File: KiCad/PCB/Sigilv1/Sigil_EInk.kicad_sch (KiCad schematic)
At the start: 6 parts, among them J2 INLAND E-PAPER HEADER (8-PIN), J3 BUZZER LOGICAL ONLY, J4 ANALOG JOYSTICK HEADER (5-PIN), J5 NEOPIXEL JEWEL 7 RGBW, U1 REMOVABLE ESP32 DEVKIT / 2 x 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

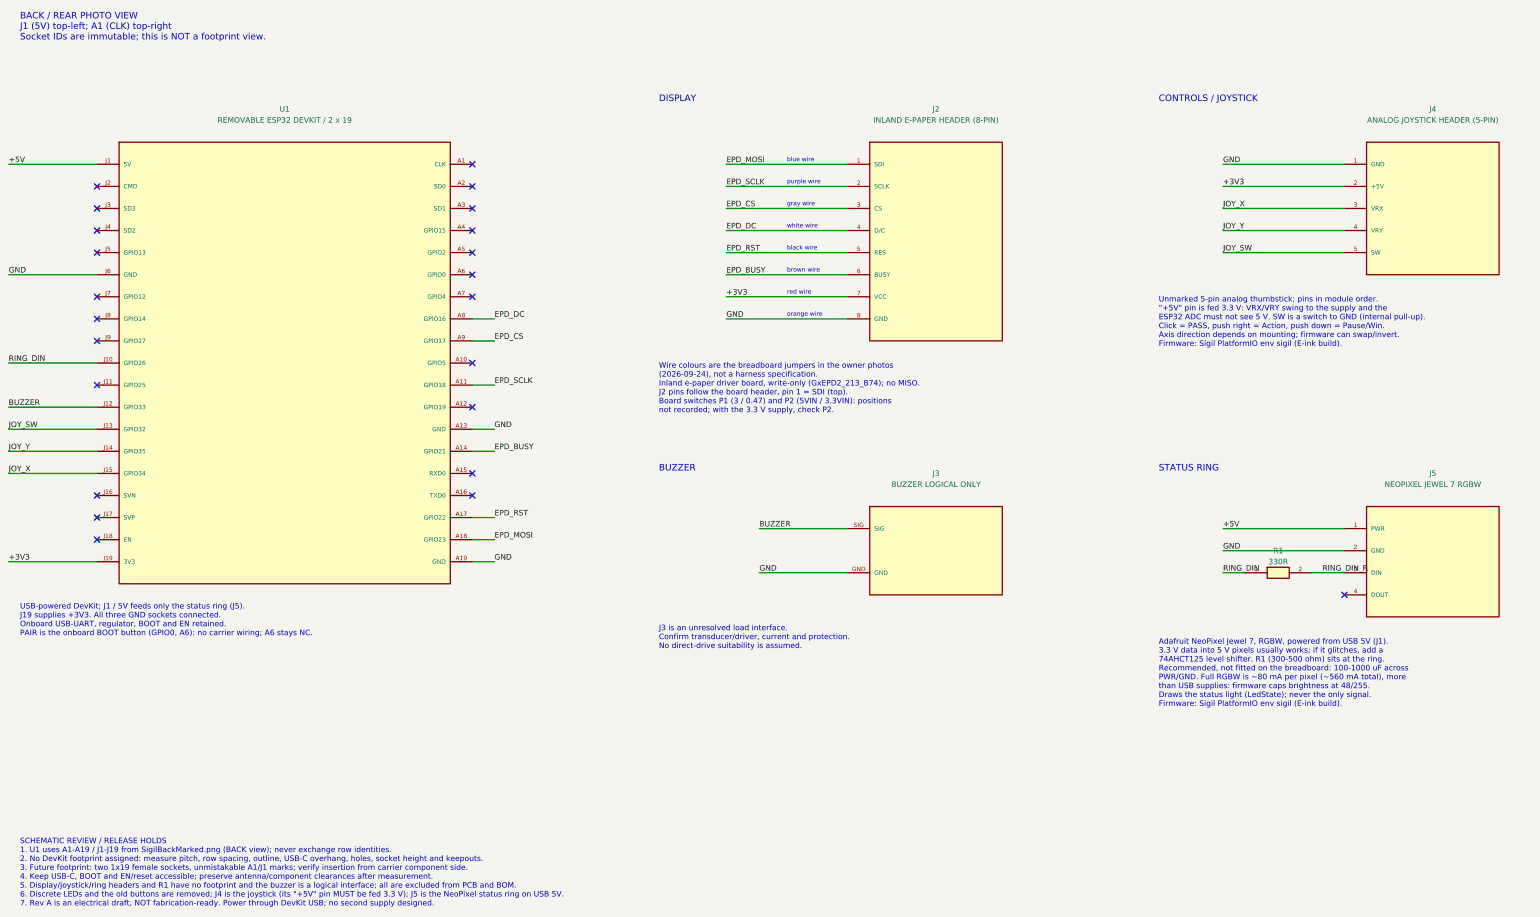
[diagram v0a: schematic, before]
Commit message: New LED Ring
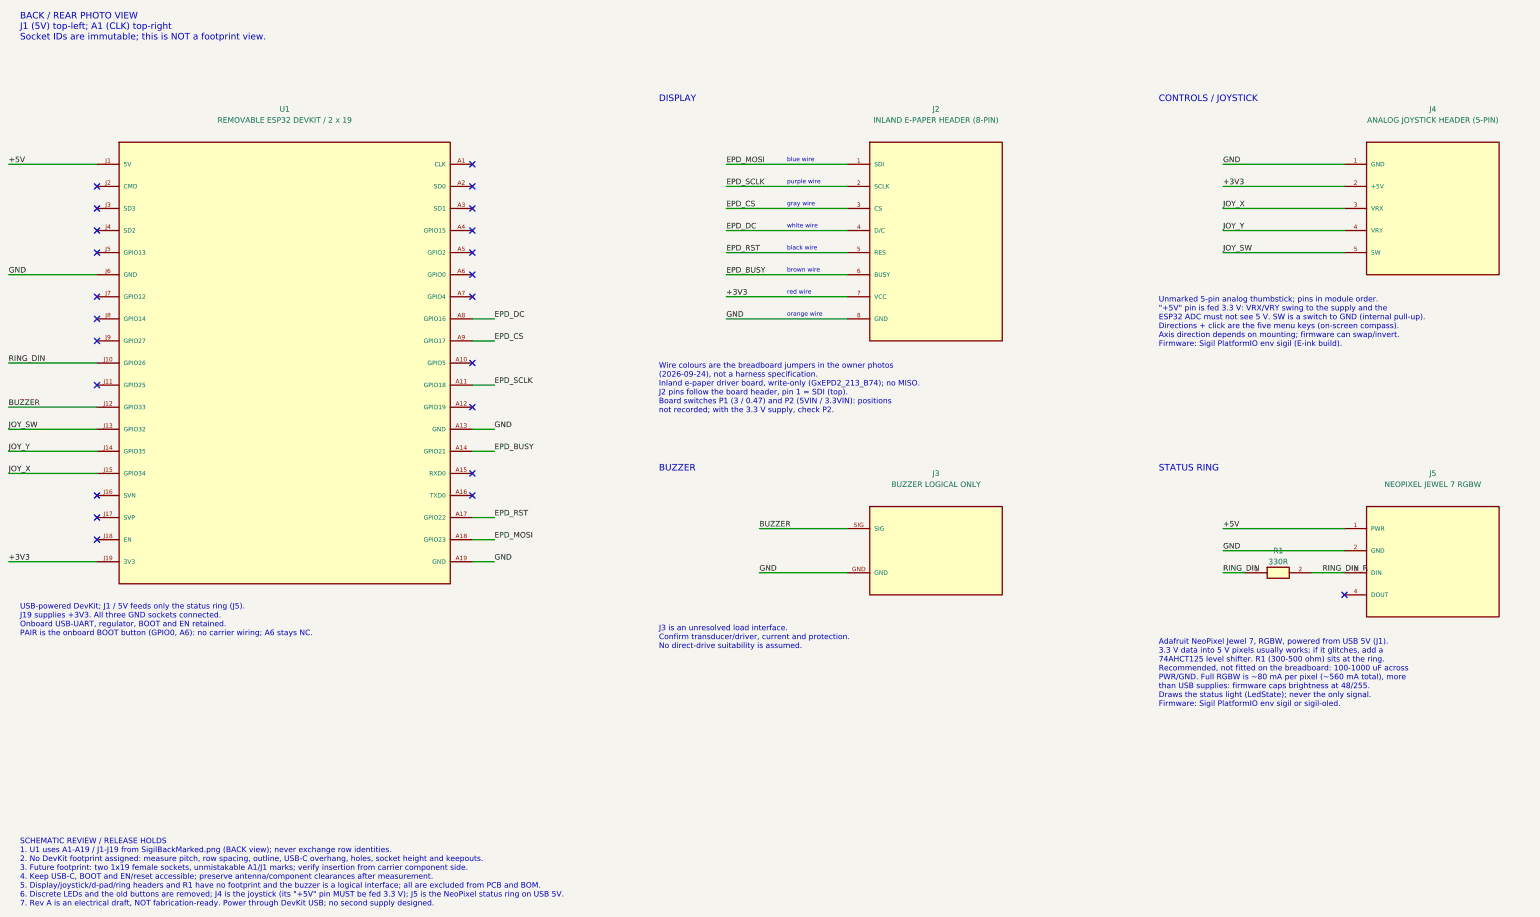
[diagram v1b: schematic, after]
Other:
- note added: "Unmarked 5-pin analog thumbstick; pins in module order. "+5V" pin is fed 3.3 V: VRX/VRY swing to the supply and the ESP32 ADC must not see 5 V. SW is a switch to GND (internal pull-up). Directions + click are the five menu keys (on-screen compass). Axis direction depends on mounting; firmware can swap/invert. Firmware: Sigil PlatformIO env sigil (E-ink build)."
- note removed: "Unmarked 5-pin analog thumbstick; pins in module order. "+5V" pin is fed 3.3 V: VRX/VRY swing to the supply and the ESP32 ADC must not see 5 V. SW is a switch to GND (internal pull-up). Click = PASS, push right = Action, push down = Pause/Win. Axis direction depends on mounting; firmware can swap/invert. Firmware: Sigil PlatformIO env sigil (E-ink build)."
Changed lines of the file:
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@@
 		(comment 1 "Rear-photo socket numbering. Joystick J4, status ring J5.")
+	)
+	(text "Adafruit NeoPixel Jewel 7, RGBW, powered from USB 5V (J1).\n3.3 V data into 5 V pixels usually works; if it glitches, add a\n74AHCT125 level shifter. R1 (300-500 ohm) sits at the ring.\nRecommended, not fitted on the breadboard: 100-1000 uF across\nPWR/GND. Full RGBW is ~80 mA per pixel (~560 mA total), more\nthan USB supplies: firmware caps brightness at 48/255.\nDraws the status light (LedState); never the only signal.\nFirmware: Sigil PlatformIO env sigil or sigil-oled."
+		(exclude_from_sim no)
+		(at 290 165.1 0)
+		(effects
+			(font
+				(size 1.27 1.27)
+			)
+			(justify left top)
+		)
 	)
 	(text "CONTROLS / JOYSTICK"
@@
 		(exclude_from_sim no)
 		(at 175 162 0)
+		(effects
+			(font
+				(size 1.27 1.27)
+			)
+			(justify left top)
+		)
+	)
+	(text "SCHEMATIC REVIEW / RELEASE HOLDS\n1. U1 uses A1-A19 / J1-J19 from SigilBackMarked.png (BACK view); never exchange row identities.\n2. No DevKit footprint assigned: measure pitch, row spacing, outline, USB-C overhang, holes, socket height and keepouts.\n3. Future footprint: two 1x19 female sockets, unmistakable A1/J1 marks; verify insertion from carrier component side.\n4. Keep USB-C, BOOT and EN/reset accessible; preserve antenna/component clearances after measurement.\n5. Display/joystick/d-pad/ring headers and R1 have no footprint and the buzzer is a logical interface; all are excluded from PCB and BOM.\n6. Discrete LEDs and the old buttons are removed; J4 is the joystick (its \"+5V\" pin MUST be fed 3.3 V); J5 is the NeoPixel status ring on USB 5V.\n7. Rev A is an electrical draft, NOT fabrication-ready. Power through DevKit USB; no second supply designed."
+		(exclude_from_sim no)
+		(at 28 211 0)
 		(effects
 			(font
@@
 		)
 	)
-	(text "Adafruit NeoPixel Jewel 7, RGBW, powered from USB 5V (J1).\n3.3 V data into 5 V pixels usually works; if it glitches, add a\n74AHCT125 level shifter. R1 (300-500 ohm) sits at the ring.\nRecommended, not fitted on the breadboard: 100-1000 uF across\nPWR/GND. Full RGBW is ~80 mA per pixel (~560 mA total), more\nthan USB supplies: firmware caps brightness at 48/255.\nDraws the status light (LedState); never the only signal.\nFirmware: Sigil PlatformIO env sigil (E-ink build)."
-		(exclude_from_sim no)
-		(at 290 165.1 0)
-		(effects
-			(font
-				(size 1.27 1.27)
-			)
-			(justify left top)
-		)
-	)
 	(text "BACK / REAR PHOTO VIEW\nJ1 (5V) top-left; A1 (CLK) top-right\nSocket IDs are immutable; this is NOT a footprint view."
 		(exclude_from_sim no)
@@
 			(font
 				(size 1 1)
-			)
-			(justify left top)
-		)
-	)
-	(text "SCHEMATIC REVIEW / RELEASE HOLDS\n1. U1 uses A1-A19 / J1-J19 from SigilBackMarked.png (BACK view); never exchange row identities.\n2. No DevKit footprint assigned: measure pitch, row spacing, outline, USB-C overhang, holes, socket height and keepouts.\n3. Future footprint: two 1x19 female sockets, unmistakable A1/J1 marks; verify insertion from carrier component side.\n4. Keep USB-C, BOOT and EN/reset accessible; preserve antenna/component clearances after measurement.\n5. Display/joystick/ring headers and R1 have no footprint and the buzzer is a logical interface; all are excluded from PCB and BOM.\n6. Discrete LEDs and the old buttons are removed; J4 is the joystick (its \"+5V\" pin MUST be fed 3.3 V); J5 is the NeoPixel status ring on USB 5V.\n7. Rev A is an electrical draft, NOT fabrication-ready. Power through DevKit USB; no second supply designed."
-		(exclude_from_sim no)
-		(at 28 211 0)
-		(effects
-			(font
-				(size 1.27 1.27)
 			)
 			(justify left top)
@@
 			(font
 				(size 1 1)
-			)
-			(justify left top)
-		)
-	)
-	(text "Unmarked 5-pin analog thumbstick; pins in module order.\n\"+5V\" pin is fed 3.3 V: VRX/VRY swing to the supply and the\nESP32 ADC must not see 5 V. SW is a switch to GND (internal pull-up).\nClick = PASS, push right = Action, push down = Pause/Win.\nAxis direction depends on mounting; firmware can swap/invert.\nFirmware: Sigil PlatformIO env sigil (E-ink build)."
-		(exclude_from_sim no)
-		(at 290 86.36 0)
-		(effects
-			(font
-				(size 1.27 1.27)
 			)
 			(justify left top)
@@
 			)
 			(justify left top)
+		)
+	)
+	(text "Unmarked 5-pin analog thumbstick; pins in module order.\n\"+5V\" pin is fed 3.3 V: VRX/VRY swing to the supply and the\nESP32 ADC must not see 5 V. SW is a switch to GND (internal pull-up).\nDirections + click are the five menu keys (on-screen compass).\nAxis direction depends on mounting; firmware can swap/invert.\nFirmware: Sigil PlatformIO env sigil (E-ink build)."
+		(exclude_from_sim no)
+		(at 290 86.36 0)
+		(effects
+			(font
+				(size 1.27 1.27)
+			)
+			(justify left top)
